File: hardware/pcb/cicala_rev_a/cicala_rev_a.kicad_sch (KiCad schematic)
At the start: 0 parts

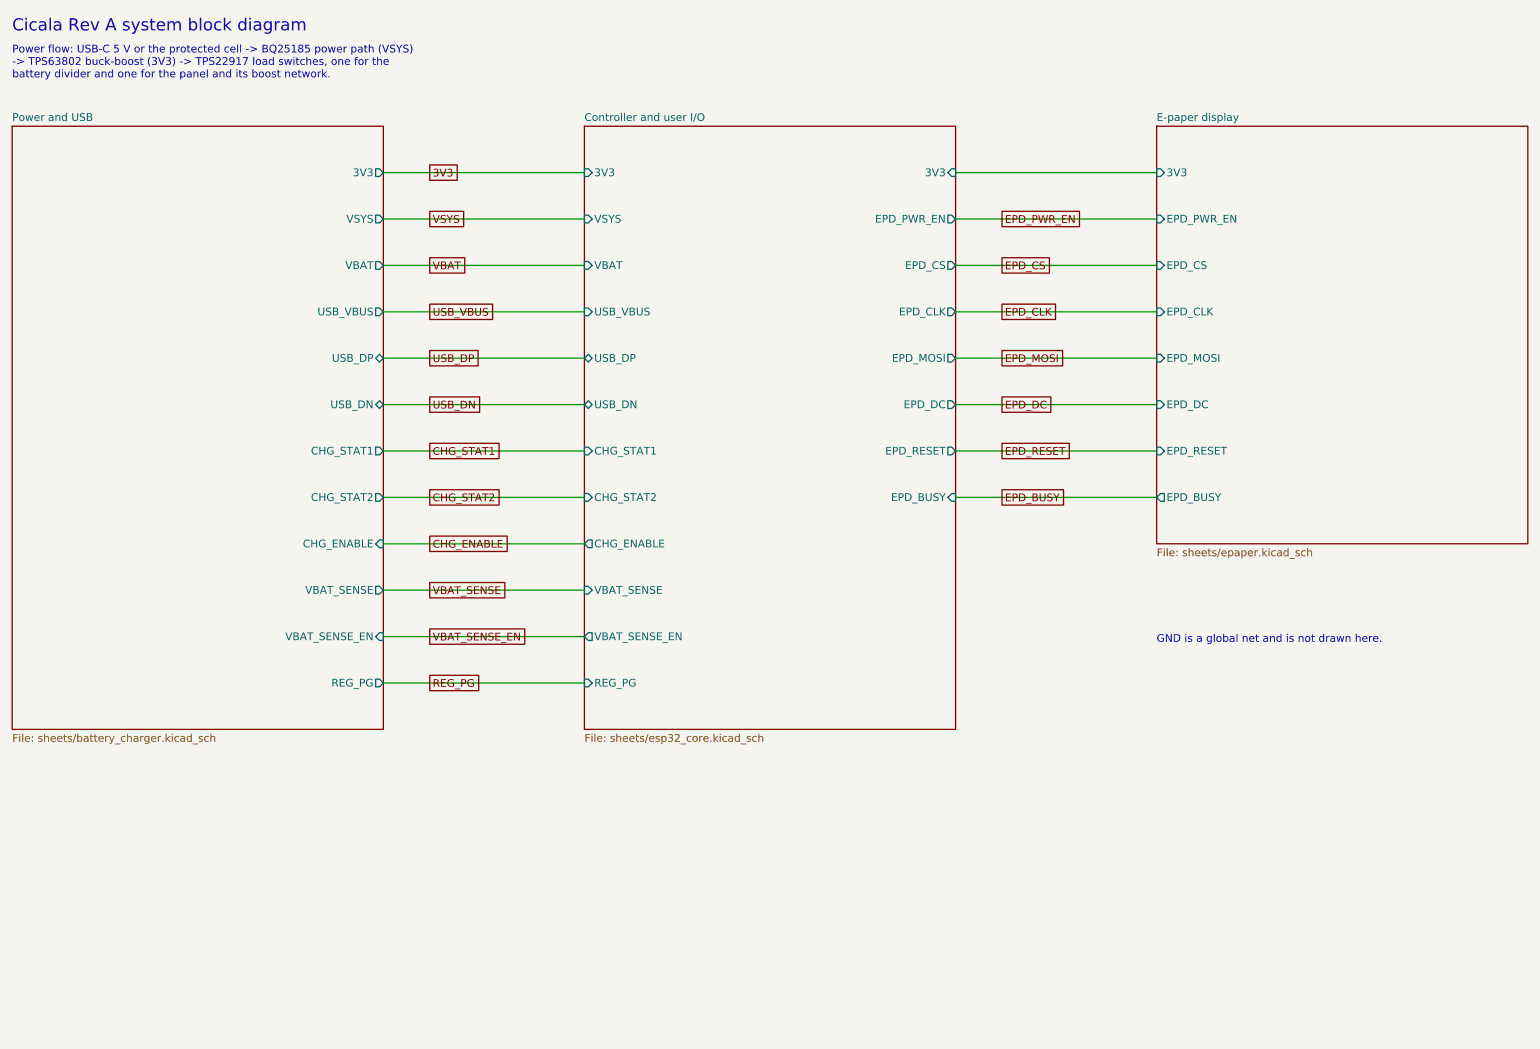
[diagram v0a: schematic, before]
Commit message: feat(hw): finalize Rev A prototype hardware and firmware
Complete the PCB and enclosure review, correct component ratings and footprints, add fitted 3D models, and export validated fabrication, assembly and print files.

Add Rev A firmware configuration, charger and power handling, USB flash/debug support, integration coverage, and build and manufacturing instructions.

Validation: zero configured ERC/DRC/parity findings; 45 PCB/export and 6 mesh tests; 14 nominal fit checks; 226 firmware cases passed with 3 platform skips; debug, charset and release/MCUboot builds; 84 Python and 101 website tests; strict docs build; prototype archive CRC/SHA256 verification. Physical prototype acceptance and factory CAM review remain pending.
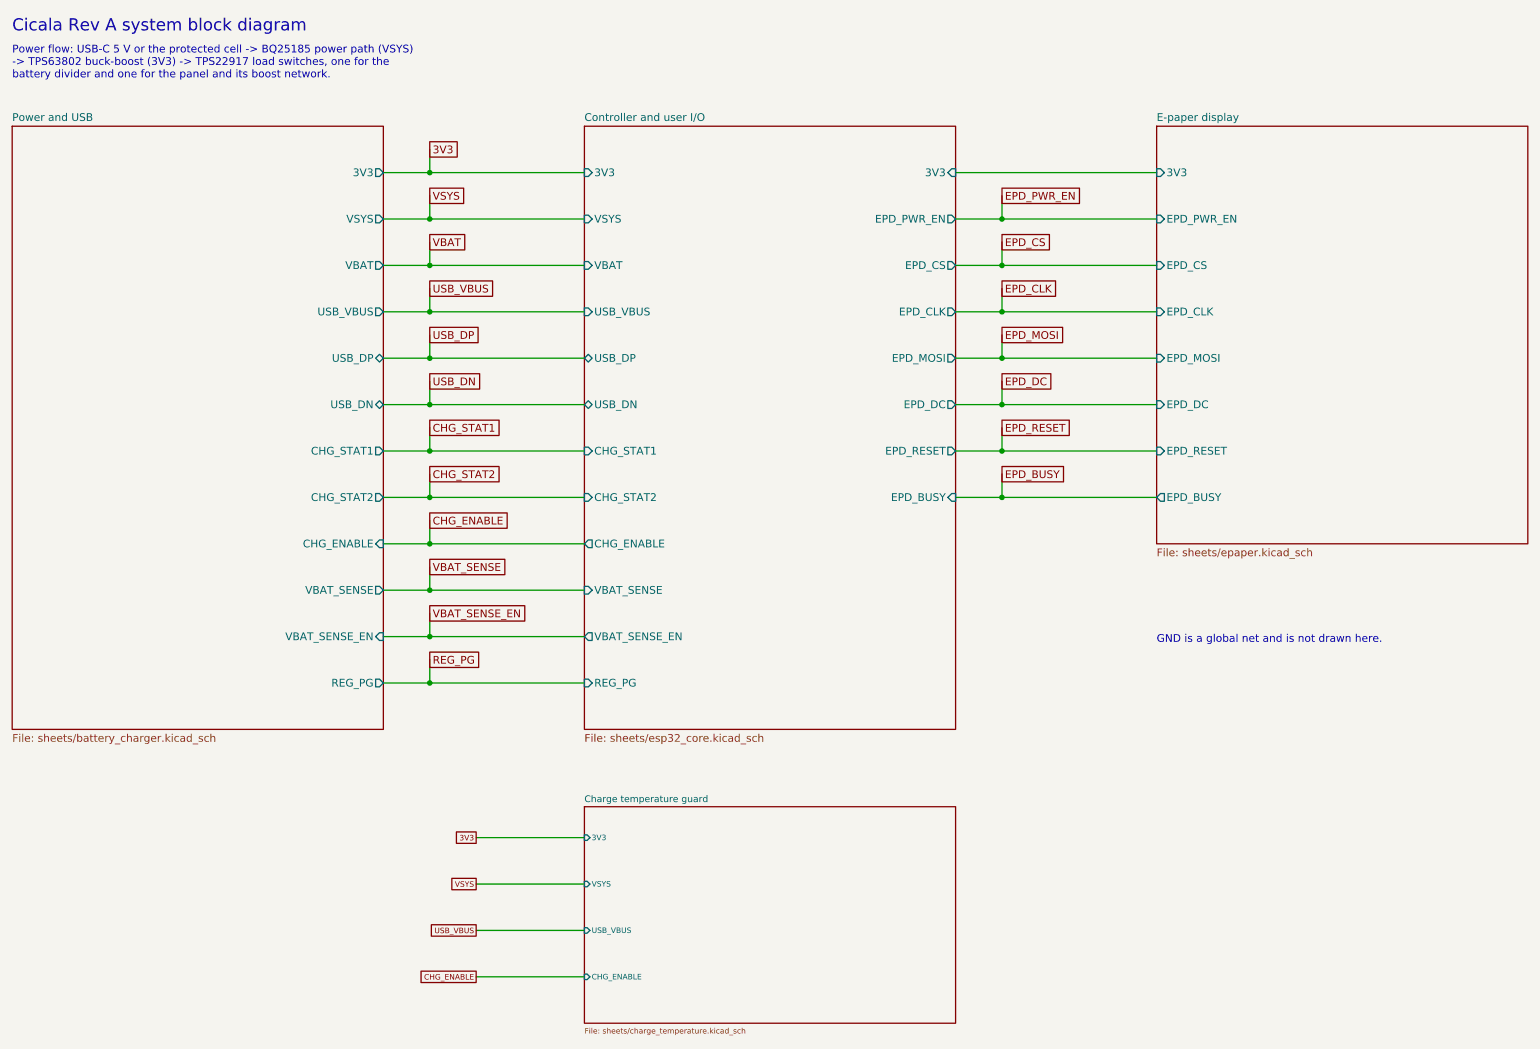
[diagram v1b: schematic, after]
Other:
- added sheet Charge temperature guard (sheets/charge_temperature.kicad_sch)
